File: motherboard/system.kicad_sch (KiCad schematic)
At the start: 32 parts, among them J10 DEBUG UART, J11 SYSTEM, J12 5V FAN, Q10 2SK3018W, Q11 AO3415A, SW1 PWR, SW2 RESET, SW3 MASK, SW4 RECOVERY, U24 SOT23 Hall Effect Sensor, U28 SPI Flash

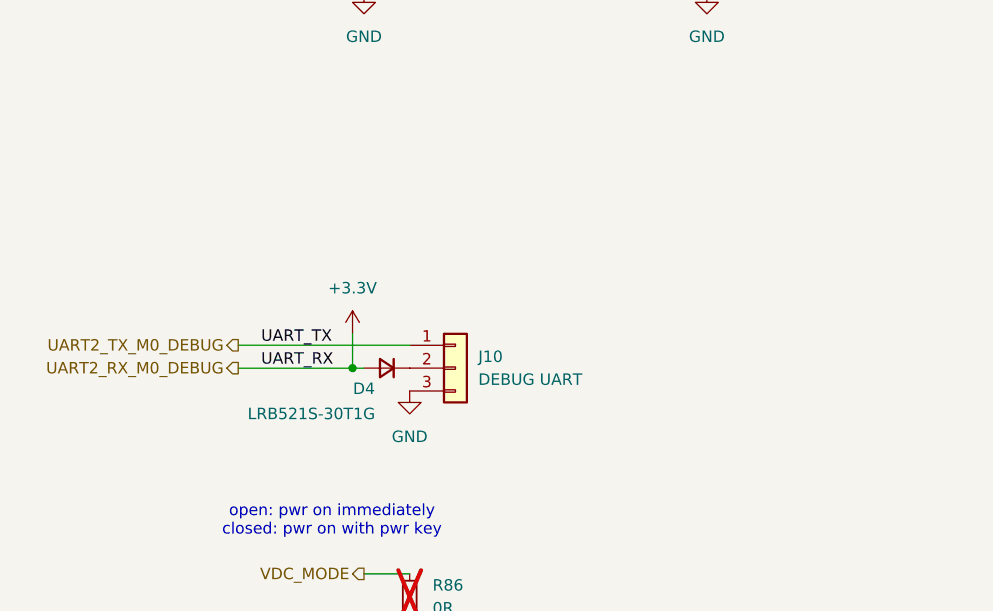
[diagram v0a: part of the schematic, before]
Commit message: created display evaluation board + layout modifications
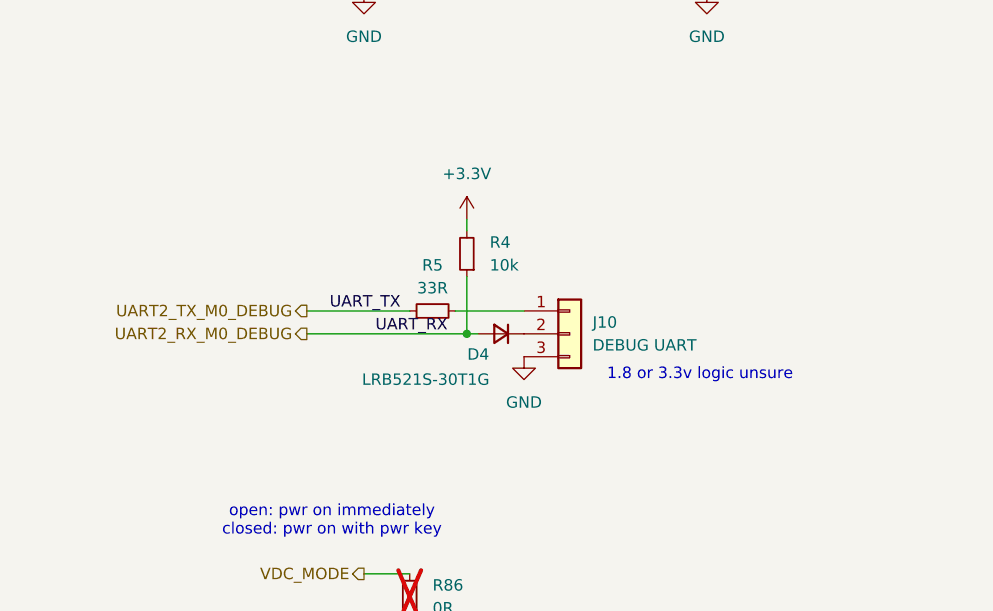
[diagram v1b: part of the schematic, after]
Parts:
- added R4: 10k, Resistor_SMD:R_0402_1005Metric, symbol Device:R_Small
- added R5: 33R, Resistor_SMD:R_0402_1005Metric, symbol Device:R_Small
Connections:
- net +3.3V: now also R4.2; no longer D4.2 (A), J11.2 (Pin_2)
- net UART2_TX_M0_DEBUG: now also R5.1; no longer J10.1 (Pin_1)
- new net: J10.1 (Pin_1), R5.2
- new net UART2_RX_M0_DEBUG: D4.2 (A), J11.2 (Pin_2), R4.1
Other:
- note added: "1.8 or 3.3v logic unsure"
- moved on the sheet: D4, J10
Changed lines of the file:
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@@
 		(comment 4 "Proof of concept board for feature verification")
 	)
+	(text "1.8 or 3.3v logic unsure"
+		(exclude_from_sim no)
+		(at 90.678 154.432 0)
+		(effects
+			(font
+				(size 1.27 1.27)
+			)
+		)
+	)
 	(text "open: pwr on immediately\nclosed: pwr on with pwr key"
 		(exclude_from_sim no)
@@
 	)
 	(junction
-		(at 52.07 153.67)
+		(at 64.77 149.86)
 		(diameter 0)
 		(color 0 0 0 0)
@@
 	(wire
 		(pts
-			(xy 52.07 153.67) (xy 53.34 153.67)
+			(xy 64.77 149.86) (xy 66.04 149.86)
 		)
 		(stroke
@@
 	(wire
 		(pts
-			(xy 52.07 153.67) (xy 52.07 149.86)
+			(xy 64.77 149.86) (xy 64.77 143.51)
 		)
 		(stroke
@@
 	(wire
 		(pts
-			(xy 39.37 151.13) (xy 58.42 151.13)
+			(xy 46.99 147.32) (xy 58.42 147.32)
 		)
 		(stroke
@@
 	(wire
 		(pts
+			(xy 64.77 138.43) (xy 64.77 137.16)
+		)
+		(stroke
+			(width 0)
+			(type default)
+		)
+	)
+	(wire
+		(pts
 			(xy 170.18 35.56) (xy 170.18 34.29)
 		)
@@
 	(wire
 		(pts
+			(xy 63.5 147.32) (xy 71.12 147.32)
+		)
+		(stroke
+			(width 0)
+			(type default)
+		)
+	)
+	(wire
+		(pts
 			(xy 129.54 29.21) (xy 129.54 26.67)
 		)
@@
 	(wire
 		(pts
-			(xy 39.37 153.67) (xy 52.07 153.67)
+			(xy 46.99 149.86) (xy 64.77 149.86)
 		)
 		(stroke
@@
 	)
 	(label "UART_TX"
-		(at 41.91 151.13 0)
+		(at 49.53 147.32 0)
 		(fields_autoplaced yes)
 		(effects
@@
 	)
 	(label "UART_RX"
-		(at 41.91 153.67 0)
+		(at 54.61 149.86 0)
 		(fields_autoplaced yes)
 		(effects
@@
 	(hierarchical_label "UART2_TX_M0_DEBUG"
 		(shape output)
-		(at 39.37 151.13 180)
+		(at 46.99 147.32 180)
 		(fields_autoplaced yes)
 		(effects
@@
 	(hierarchical_label "UART2_RX_M0_DEBUG"
 		(shape output)
-		(at 39.37 153.67 180)
+		(at 46.99 149.86 180)
 		(fields_autoplaced yes)
 		(effects
@@
 	(symbol
 		(lib_id "Device:D_Small")
-		(at 55.88 153.67 180)
+		(at 68.58 149.86 180)
 		(unit 1)
 		(exclude_from_sim no)
@@
 		(dnp no)
 		(property "Reference" "D4"
-			(at 53.34 155.956 0)
+			(at 66.04 152.146 0)
 			(effects
 				(font
@@
 		)
 		(property "Value" "LRB521S-30T1G"
-			(at 47.498 158.75 0)
+			(at 60.198 154.94 0)
 			(effects
 				(font
@@
 		)
 		(property "Footprint" "Diode_SMD:D_SOD-523"
-			(at 55.88 153.67 90)
+			(at 68.58 149.86 90)
 			(effects
 				(font
@@
 		)
 		(property "Datasheet" "~"
-			(at 55.88 153.67 90)
+			(at 68.58 149.86 90)
 			(effects
 				(font
@@
 		)
 		(property "Description" "Diode, small symbol"
-			(at 55.88 153.67 0)
+			(at 68.58 149.86 0)
 			(effects
 				(font
@@
 		)
 		(property "Sim.Device" "D"
-			(at 55.88 153.67 0)
+			(at 68.58 149.86 0)
 			(effects
 				(font
@@
 		)
 		(property "Sim.Pins" "1=K 2=A"
-			(at 55.88 153.67 0)
+			(at 68.58 149.86 0)
 			(effects
 				(font
@@
 	(symbol
 		(lib_id "Device:R_Small")
+		(at 64.77 140.97 180)
+		(unit 1)
+		(exclude_from_sim no)
+		(in_bom yes)
+		(on_board yes)
+		(dnp no)
+		(fields_autoplaced yes)
+		(property "Reference" "R4"
+			(at 67.31 139.6999 0)
+			(effects
+				(font
+					(size 1.27 1.27)
+				)
+				(justify right)
+			)
+		)
+		(property "Value" "10k"
+			(at 67.31 142.2399 0)
+			(effects
+				(font
+					(size 1.27 1.27)
+				)
+				(justify right)
+			)
+		)
+		(property "Footprint" "Resistor_SMD:R_0402_1005Metric"
+			(at 64.77 140.97 0)
+			(effects
+				(font
+					(size 1.27 1.27)
+				)
+				(hide yes)
+			)
+		)
+		(property "Datasheet" "~"
+			(at 64.77 140.97 0)
+			(effects
+				(font
+					(size 1.27 1.27)
+				)
+				(hide yes)
+			)
+		)
+		(property "Description" "Resistor, small symbol"
+			(at 64.77 140.97 0)
+			(effects
+				(font
+					(size 1.27 1.27)
+				)
+				(hide yes)
+			)
+		)
+		(pin "1"
+		)
+		(pin "2"
+		)
+		(instances
+			(project "motherboard"
+				(path "/025fe4d1-0305-4b34-be04-f8d9818125a4/d2371120-9201-4f7f-a684-821b8780a78d"
+					(reference "R4")
+					(unit 1)
+				)
+			)
+		)
+	)
+	(symbol
+		(lib_id "Device:R_Small")
 		(at 64.77 57.15 90)
 		(unit 1)
@@
 	)
 	(symbol
+		(lib_id "Device:R_Small")
+		(at 60.96 147.32 90)
+		(unit 1)
+		(exclude_from_sim no)
+		(in_bom yes)
+		(on_board yes)
+		(dnp no)
+		(fields_autoplaced yes)
+		(property "Reference" "R5"
+			(at 60.96 142.24 90)
+			(effects
+				(font
+					(size 1.27 1.27)
+				)
+			)
+		)
+		(property "Value" "33R"
+			(at 60.96 144.78 90)
+			(effects
+				(font
+					(size 1.27 1.27)
+				)
+			)
+		)
+		(property "Footprint" "Resistor_SMD:R_0402_1005Metric"
+			(at 60.96 147.32 0)
+			(effects
+				(font
+					(size 1.27 1.27)
+				)
+				(hide yes)
+			)
+		)
+		(property "Datasheet" "~"
+			(at 60.96 147.32 0)
+			(effects
+				(font
+					(size 1.27 1.27)
+				)
+				(hide yes)
+			)
+		)
+		(property "Description" "Resistor, small symbol"
+			(at 60.96 147.32 0)
+			(effects
+				(font
+					(size 1.27 1.27)
+				)
+				(hide yes)
+			)
+		)
+		(pin "2"
+		)
+		(pin "1"
+		)
+		(instances
+			(project "motherboard"
+				(path "/025fe4d1-0305-4b34-be04-f8d9818125a4/d2371120-9201-4f7f-a684-821b8780a78d"
+					(reference "R5")
+					(unit 1)
+				)
+			)
+		)
+	)
+	(symbol
 		(lib_id "power:+3.3V")
-		(at 52.07 149.86 0)
+		(at 64.77 137.16 0)
 		(unit 1)
 		(exclude_from_sim no)
@@
 		(fields_autoplaced yes)
 		(property "Reference" "#PWR065"
-			(at 52.07 153.67 0)
+			(at 64.77 140.97 0)
 			(effects
 				(font
@@
 		)
 		(property "Value" "+3.3V"
-			(at 52.07 144.78 0)
+			(at 64.77 132.08 0)
 			(effects
 				(font
@@
 		)
 		(property "Footprint" ""
-			(at 52.07 149.86 0)
+			(at 64.77 137.16 0)
 			(effects
 				(font
@@
 		)
 		(property "Datasheet" ""
-			(at 52.07 149.86 0)
+			(at 64.77 137.16 0)
 			(effects
 				(font
@@
 		)
 		(property "Description" "Power symbol creates a global label with name \"+3.3V\""
-			(at 52.07 149.86 0)
+			(at 64.77 137.16 0)
 			(effects
 				(font
@@
 	(symbol
 		(lib_id "Connector_Generic:Conn_01x03")
-		(at 63.5 153.67 0)
+		(at 76.2 149.86 0)
 		(unit 1)
 		(exclude_from_sim no)
@@
 		(fields_autoplaced yes)
 		(property "Reference" "J10"
-			(at 66.04 152.3999 0)
+			(at 78.74 148.5899 0)
 			(effects
 				(font
@@
 		)
 		(property "Value" "DEBUG UART"
-			(at 66.04 154.9399 0)
+			(at 78.74 151.1299 0)
 			(effects
 				(font
@@
 		)
 		(property "Footprint" "Connector_PinHeader_2.54mm:PinHeader_1x03_P2.54mm_Vertical"
-			(at 63.5 153.67 0)
+			(at 76.2 149.86 0)
 			(effects
 				(font
@@
 		)
 		(property "Datasheet" "~"
-			(at 63.5 153.67 0)
+			(at 76.2 149.86 0)
 			(effects
 				(font
@@
 		)
 		(property "Description" "Generic connector, single row, 01x03, script generated (kicad-library-utils/schlib/autogen/connector/)"
-			(at 63.5 153.67 0)
+			(at 76.2 149.86 0)
 			(effects
 				(font
@@
 	(symbol
 		(lib_id "power:GND")
-		(at 58.42 156.21 0)
+		(at 71.12 152.4 0)
 		(unit 1)
 		(exclude_from_sim no)
@@
 		(fields_autoplaced yes)
 		(property "Reference" "#PWR066"
-			(at 58.42 162.56 0)
+			(at 71.12 158.75 0)
 			(effects
 				(font
@@
 		)
 		(property "Value" "GND"
-			(at 58.42 161.29 0)
+			(at 71.12 157.48 0)
 			(effects
 				(font
@@
 		)
 		(property "Footprint" ""
-			(at 58.42 156.21 0)
+			(at 71.12 152.4 0)
 			(effects
 				(font
@@
 		)
 		(property "Datasheet" ""
-			(at 58.42 156.21 0)
+			(at 71.12 152.4 0)
 			(effects
 				(font
@@
 		)
 		(property "Description" "Power symbol creates a global label with name \"GND\" , ground"
-			(at 58.42 156.21 0)
+			(at 71.12 152.4 0)
 			(effects
 				(font

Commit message: motherboard net labeling and impedance matching
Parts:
- removed C70: 0.1uF, Capacitor_SMD:C_0402_1005Metric, symbol Device:C_Small
- removed U24: SOT23 Hall Effect Sensor, Package_TO_SOT_SMD:SOT-23, symbol Sensor_Magnetic:SM351LT
- added J7: HALL SWITCH, 6P_05mm_FPC:FPC-SMD_6P-P0.50_XUNPU_FPC-05F-6PH20, symbol Connector_Generic_MountingPin:Conn_01x06_MountingPin
- added TP1: PWRON, symbol Connector:TestPoint
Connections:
- net +3.3V: now also J7.1 (Pin_1)
- net GND: now also J7.3 (Pin_3), J7.MP (MountPin)
- net GPIO4_C2/HALL_OUT: now also J7.2 (Pin_2)
- net PWRON_L_IN: now also TP1.1
- no-connect marks 0 -> 3

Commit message: starting motherboard v0.2
lessons from display eval v1
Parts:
- R86: now fitted
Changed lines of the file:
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@@
 		(in_bom yes)
 		(on_board yes)
-		(dnp yes)
+		(dnp no)
 		(fields_autoplaced yes)
 		(property "Reference" "R86"

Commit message: v0.2 layout
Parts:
- TP1: footprint (none) -> TestPoint:TestPoint_THTPad_1.0x1.0mm_Drill0.5mm
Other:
- moved on the sheet: D4, J10, R4, R5, R86
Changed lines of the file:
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@@
 	(text "1.8 or 3.3v logic unsure"
 		(exclude_from_sim no)
-		(at 90.678 154.432 0)
+		(at 107.188 141.732 0)
 		(effects
 			(font
@@
 	(text "open: pwr on immediately\nclosed: pwr on with pwr key"
 		(exclude_from_sim no)
-		(at 49.784 170.688 0)
+		(at 66.294 157.988 0)
 		(effects
 			(font
@@
 	)
 	(junction
-		(at 64.77 149.86)
+		(at 81.28 137.16)
 		(diameter 0)
 		(color 0 0 0 0)
@@
 	(wire
 		(pts
-			(xy 53.34 176.53) (xy 58.42 176.53)
+			(xy 69.85 163.83) (xy 74.93 163.83)
 		)
 		(stroke
@@
 	(wire
 		(pts
-			(xy 64.77 149.86) (xy 66.04 149.86)
+			(xy 81.28 137.16) (xy 82.55 137.16)
 		)
 		(stroke
@@
 	(wire
 		(pts
-			(xy 64.77 149.86) (xy 64.77 143.51)
+			(xy 81.28 137.16) (xy 81.28 130.81)
 		)
 		(stroke
@@
 	(wire
 		(pts
-			(xy 46.99 147.32) (xy 58.42 147.32)
+			(xy 63.5 134.62) (xy 74.93 134.62)
 		)
 		(stroke
@@
 	(wire
 		(pts
-			(xy 64.77 138.43) (xy 64.77 137.16)
+			(xy 81.28 125.73) (xy 81.28 124.46)
 		)
 		(stroke
@@
 	(wire
 		(pts
-			(xy 63.5 147.32) (xy 71.12 147.32)
+			(xy 80.01 134.62) (xy 87.63 134.62)
 		)
 		(stroke
@@
 	(wire
 		(pts
-			(xy 46.99 149.86) (xy 64.77 149.86)
+			(xy 63.5 137.16) (xy 81.28 137.16)
 		)
 		(stroke
@@
 	)
 	(label "UART_TX"
-		(at 49.53 147.32 0)
+		(at 66.04 134.62 0)
 		(fields_autoplaced yes)
 		(effects
@@
 	)
 	(label "UART_RX"
-		(at 54.61 149.86 0)
+		(at 71.12 137.16 0)
 		(fields_autoplaced yes)
 		(effects
@@
 	(hierarchical_label "UART2_TX_M0_DEBUG"
 		(shape output)
-		(at 46.99 147.32 180)
+		(at 63.5 134.62 180)
 		(fields_autoplaced yes)
 		(effects
@@
 	(hierarchical_label "VDC_MODE"
 		(shape output)
-		(at 53.34 176.53 180)
+		(at 69.85 163.83 180)
 		(fields_autoplaced yes)
 		(effects
@@
 	(hierarchical_label "UART2_RX_M0_DEBUG"
 		(shape output)
-		(at 46.99 149.86 180)
+		(at 63.5 137.16 180)
 		(fields_autoplaced yes)
 		(effects
@@
 	(symbol
 		(lib_id "Device:D_Small")
-		(at 68.58 149.86 180)
+		(at 85.09 137.16 180)
 		(unit 1)
 		(exclude_from_sim no)
@@
 		(dnp no)
 		(property "Reference" "D4"
-			(at 66.04 152.146 0)
+			(at 82.55 139.446 0)
 			(effects
 				(font
@@
 		)
 		(property "Value" "LRB521S-30T1G"
-			(at 60.198 154.94 0)
+			(at 76.708 142.24 0)
 			(effects
 				(font
@@
 		)
 		(property "Footprint" "Diode_SMD:D_SOD-523"
-			(at 68.58 149.86 90)
+			(at 85.09 137.16 90)
 			(effects
 				(font
@@
 		)
 		(property "Datasheet" "~"
-			(at 68.58 149.86 90)
+			(at 85.09 137.16 90)
 			(effects
 				(font
@@
 		)
 		(property "Description" "Diode, small symbol"
-			(at 68.58 149.86 0)
+			(at 85.09 137.16 0)
 			(effects
 				(font
@@
 		)
 		(property "Sim.Device" "D"
-			(at 68.58 149.86 0)
+			(at 85.09 137.16 0)
 			(effects
 				(font
@@
 		)
 		(property "Sim.Pins" "1=K 2=A"
-			(at 68.58 149.86 0)
+			(at 85.09 137.16 0)
 			(effects
 				(font
@@
 	(symbol
 		(lib_id "power:GND")
-		(at 58.42 181.61 0)
+		(at 74.93 168.91 0)
 		(unit 1)
 		(exclude_from_sim no)
@@
 		(fields_autoplaced yes)
 		(property "Reference" "#PWR067"
-			(at 58.42 187.96 0)
+			(at 74.93 175.26 0)
 			(effects
 				(font
@@
 		)
 		(property "Value" "GND"
-			(at 58.42 186.69 0)
+			(at 74.93 173.99 0)
 			(effects
 				(font
@@
 		)
 		(property "Footprint" ""
-			(at 58.42 181.61 0)
+			(at 74.93 168.91 0)
 			(effects
 				(font
@@
 		)
 		(property "Datasheet" ""
-			(at 58.42 181.61 0)
+			(at 74.93 168.91 0)
 			(effects
 				(font
@@
 		)
 		(property "Description" "Power symbol creates a global label with name \"GND\" , ground"
-			(at 58.42 181.61 0)
+			(at 74.93 168.91 0)
 			(effects
 				(font
@@
 	(symbol
 		(lib_id "Device:R_Small")
-		(at 64.77 140.97 180)
+		(at 81.28 128.27 180)
 		(unit 1)
 		(exclude_from_sim no)
@@
 		(fields_autoplaced yes)
 		(property "Reference" "R4"
-			(at 67.31 139.6999 0)
+			(at 83.82 126.9999 0)
 			(effects
 				(font
@@
 		)
 		(property "Value" "10k"
-			(at 67.31 142.2399 0)
+			(at 83.82 129.5399 0)
 			(effects
 				(font
@@
 		)
 		(property "Footprint" "Resistor_SMD:R_0402_1005Metric"
-			(at 64.77 140.97 0)
+			(at 81.28 128.27 0)
 			(effects
 				(font
@@
 		)
 		(property "Datasheet" "~"
-			(at 64.77 140.97 0)
+			(at 81.28 128.27 0)
 			(effects
 				(font
@@
 		)
 		(property "Description" "Resistor, small symbol"
-			(at 64.77 140.97 0)
+			(at 81.28 128.27 0)
 			(effects
 				(font
@@
 	(symbol
 		(lib_id "Device:R_Small")
-		(at 58.42 179.07 0)
+		(at 74.93 166.37 0)
 		(unit 1)
 		(exclude_from_sim no)
@@
 		(fields_autoplaced yes)
 		(property "Reference" "R86"
-			(at 60.96 177.7999 0)
+			(at 77.47 165.0999 0)
 			(effects
 				(font
@@
 		)
 		(property "Value" "0R"
-			(at 60.96 180.3399 0)
+			(at 77.47 167.6399 0)
 			(effects
 				(font
@@
 		)
 		(property "Footprint" "Jumper:SolderJumper-2_P1.3mm_Open_TrianglePad1.0x1.5mm"
-			(at 58.42 179.07 0)
+			(at 74.93 166.37 0)
 			(effects
 				(font
@@
 		)
 		(property "Datasheet" "~"
-			(at 58.42 179.07 0)
+			(at 74.93 166.37 0)
 			(effects
 				(font
@@
 		)
 		(property "Description" "Resistor, small symbol"
-			(at 58.42 179.07 0)
+			(at 74.93 166.37 0)
 			(effects
 				(font
@@
 	(symbol
 		(lib_id "Device:R_Small")
-		(at 60.96 147.32 90)
+		(at 77.47 134.62 90)
 		(unit 1)
 		(exclude_from_sim no)
@@
 		(fields_autoplaced yes)
 		(property "Reference" "R5"
-			(at 60.96 142.24 90)
+			(at 77.47 129.54 90)
 			(effects
 				(font
@@
 		)
 		(property "Value" "33R"
-			(at 60.96 144.78 90)
+			(at 77.47 132.08 90)
 			(effects
 				(font
@@
 		)
 		(property "Footprint" "Resistor_SMD:R_0402_1005Metric"
-			(at 60.96 147.32 0)
+			(at 77.47 134.62 0)
 			(effects
 				(font
@@
 		)
 		(property "Datasheet" "~"
-			(at 60.96 147.32 0)
+			(at 77.47 134.62 0)
 			(effects
 				(font
@@
 		)
 		(property "Description" "Resistor, small symbol"
-			(at 60.96 147.32 0)
+			(at 77.47 134.62 0)
 			(effects
 				(font
@@
 	(symbol
 		(lib_id "power:+3.3V")
-		(at 64.77 137.16 0)
+		(at 81.28 124.46 0)
 		(unit 1)
 		(exclude_from_sim no)
@@
 		(fields_autoplaced yes)
 		(property "Reference" "#PWR065"
-			(at 64.77 140.97 0)
+			(at 81.28 128.27 0)
 			(effects
 				(font
@@
 		)
 		(property "Value" "+3.3V"
-			(at 64.77 132.08 0)
+			(at 81.28 119.38 0)
 			(effects
 				(font
@@
 		)
 		(property "Footprint" ""
-			(at 64.77 137.16 0)
+			(at 81.28 124.46 0)
 			(effects
 				(font
@@
 		)
 		(property "Datasheet" ""
-			(at 64.77 137.16 0)
+			(at 81.28 124.46 0)
 			(effects
 				(font
@@
 		)
 		(property "Description" "Power symbol creates a global label with name \"+3.3V\""
-			(at 64.77 137.16 0)
+			(at 81.28 124.46 0)
 			(effects
 				(font
@@
 	(symbol
 		(lib_id "Connector_Generic:Conn_01x03")
-		(at 76.2 149.86 0)
+		(at 92.71 137.16 0)
 		(unit 1)
 		(exclude_from_sim no)
@@
 		(fields_autoplaced yes)
 		(property "Reference" "J10"
-			(at 78.74 148.5899 0)
+			(at 95.25 135.8899 0)
 			(effects
 				(font
@@
 		)
 		(property "Value" "DEBUG UART"
-			(at 78.74 151.1299 0)
+			(at 95.25 138.4299 0)
 			(effects
 				(font
@@
 		)
 		(property "Footprint" "Connector_PinHeader_2.54mm:PinHeader_1x03_P2.54mm_Vertical"
-			(at 76.2 149.86 0)
+			(at 92.71 137.16 0)
 			(effects
 				(font
@@
 		)
 		(property "Datasheet" "~"
-			(at 76.2 149.86 0)
+			(at 92.71 137.16 0)
 			(effects
 				(font
@@
 		)
 		(property "Description" "Generic connector, single row, 01x03, script generated (kicad-library-utils/schlib/autogen/connector/)"
-			(at 76.2 149.86 0)
+			(at 92.71 137.16 0)
 			(effects
 				(font
@@
 			)
 		)
-		(property "Footprint" ""
+		(property "Footprint" "TestPoint:TestPoint_THTPad_1.0x1.0mm_Drill0.5mm"
 			(at 77.47 49.53 0)
 			(effects
@@
 	(symbol
 		(lib_id "power:GND")
-		(at 71.12 152.4 0)
+		(at 87.63 139.7 0)
 		(unit 1)
 		(exclude_from_sim no)
@@
 		(fields_autoplaced yes)
 		(property "Reference" "#PWR066"
-			(at 71.12 158.75 0)
+			(at 87.63 146.05 0)
 			(effects
 				(font
@@
 		)
 		(property "Value" "GND"
-			(at 71.12 157.48 0)
+			(at 87.63 144.78 0)
 			(effects
 				(font
@@
 		)
 		(property "Footprint" ""
-			(at 71.12 152.4 0)
+			(at 87.63 139.7 0)
 			(effects
 				(font
@@
 		)
 		(property "Datasheet" ""
-			(at 71.12 152.4 0)
+			(at 87.63 139.7 0)
 			(effects
 				(font
@@
 		)
 		(property "Description" "Power symbol creates a global label with name \"GND\" , ground"
-			(at 71.12 152.4 0)
+			(at 87.63 139.7 0)
 			(effects
 				(font

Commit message: v0.2 75 routes left!
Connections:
- net +3.3V: no longer J7.1 (Pin_1)
- new net +3.3V_PCIE: J7.1 (Pin_1)
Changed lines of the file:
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@@
 		(at 154.94 90.17)
+	)
+	(bus_entry
+		(at 66.04 73.66)
+		(size 2.54 2.54)
+		(stroke
+			(width 0)
+			(type default)
+		)
 	)
 	(wire
@@
 			)
 			(justify left bottom)
+		)
+	)
+	(global_label "+3.3V_PCIE"
+		(shape input)
+		(at 154.94 77.47 180)
+		(fields_autoplaced yes)
+		(effects
+			(font
+				(size 1.27 1.27)
+			)
+			(justify right)
+		)
+		(property "Intersheetrefs" "${INTERSHEET_REFS}"
+			(at 141.0086 77.47 0)
+			(effects
+				(font
+					(size 1.27 1.27)
+				)
+				(justify right)
+				(hide yes)
+			)
 		)
 	)
@@
 					(unit 1)
 				)
-			)
-		)
-	)
-	(symbol
-		(lib_id "power:+3.3V")
-		(at 154.94 77.47 0)
-		(unit 1)
-		(exclude_from_sim no)
-		(in_bom yes)
-		(on_board yes)
-		(dnp no)
-		(fields_autoplaced yes)
-		(property "Reference" "#PWR074"
-			(at 154.94 81.28 0)
-			(effects
-				(font
-					(size 1.27 1.27)
-				)
-				(hide yes)
-			)
-		)
-		(property "Value" "+3.3V"
-			(at 154.94 72.39 0)
-			(effects
-				(font
-					(size 1.27 1.27)
-				)
-			)
-		)
-		(property "Footprint" ""
-			(at 154.94 77.47 0)
-			(effects
-				(font
-					(size 1.27 1.27)
-				)
-				(hide yes)
-			)
-		)
-		(property "Datasheet" ""
-			(at 154.94 77.47 0)
-			(effects
-				(font
-					(size 1.27 1.27)
-				)
-				(hide yes)
-			)
-		)
-		(property "Description" "Power symbol creates a global label with name \"+3.3V\""
-			(at 154.94 77.47 0)
-			(effects
-				(font
-					(size 1.27 1.27)
-				)
-				(hide yes)
-			)
-		)
-		(pin "1"
-		)
-		(instances
-			(project "motherboard"
-				(path "/025fe4d1-0305-4b34-be04-f8d9818125a4/d2371120-9201-4f7f-a684-821b8780a78d"
-					(reference "#PWR074")
-					(unit 1)
-				)

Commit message: v0.2 submitted to production
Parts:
- U28: footprint Package_SO:SOIC-8_3.9x4.9mm_P1.27mm -> Package_SON:WSON-8-1EP_6x5mm_P1.27mm_EP3.4x4.3mm
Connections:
- net +1V8: now also C90.1, C91.1, R116.1, R117.1, U28.8 (VCC)
- net +3.3V: no longer C90.1, C91.1, R116.1, R117.1, U28.8 (VCC)
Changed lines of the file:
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@@
 			)
 		)
-		(property "Value" "+3.3V"
-			(at 190.5 111.76 0)
+		(property "Value" "+1V8"
+			(at 193.04 115.5699 0)
 			(effects
 				(font
 					(size 1.27 1.27)
 				)
+				(justify left)
 			)
 		)
@@
 			)
 		)
-		(property "Footprint" "Package_SO:SOIC-8_3.9x4.9mm_P1.27mm"
+		(property "Footprint" "Package_SON:WSON-8-1EP_6x5mm_P1.27mm_EP3.4x4.3mm"
 			(at 190.5 152.4 0)
 			(effects
@@
 			)
 		)
-		(property "Value" "+3.3V"
-			(at 170.18 111.76 0)
+		(property "Value" "+1V8"
+			(at 172.72 115.5699 0)
 			(effects
 				(font
 					(size 1.27 1.27)
 				)
+				(justify left)
 			)
 		)

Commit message: mainboard v0.3 + power WIP
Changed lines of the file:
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@@
 	(title_block
 		(title "anyon e")
-		(date "2024-06-12")
-		(rev "V0.1")
+		(date "2024-09-15")
+		(rev "V0.3")
 		(company "Byran Huang")
 		(comment 4 "Proof of concept board for feature verification")
@@
 		(at 154.94 90.17)
 	)
-	(bus_entry
-		(at 66.04 73.66)
-		(size 2.54 2.54)
-		(stroke
-			(width 0)
-			(type default)
-		)
-	)
 	(wire

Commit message: preparing for motherboard v1.1
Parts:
- renumbered C32 to C42, C28 to C43, C29 to C44, C30 to C45, C31 to C46, C90 to C47, C91 to C48, D4 to D5, J12 to J11, J7 to J12, J11 to J13, J10 to J14, Q11 to Q1, Q10 to Q2, R49 to R35, R48 to R36, R47 to R37, R45 to R38, R46 to R39, R41 to R40, R42 to R41, R43 to R42, R44 to R43, R117 to R44, R116 to R45, R4 to R46, R5 to R47, R86 to R48, U28 to U17
